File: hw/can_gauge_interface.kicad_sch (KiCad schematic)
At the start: 61 parts, among them J1 Conn_02x04_Top_Bottom, J2 Analog, J3 Power debug, J4 Power debug, J5 SPI debug, J6 I^{2}C debug, J7 CAN debug, J8 SWD, U1 STM32C092CBT6, U2 TPS5430DDA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

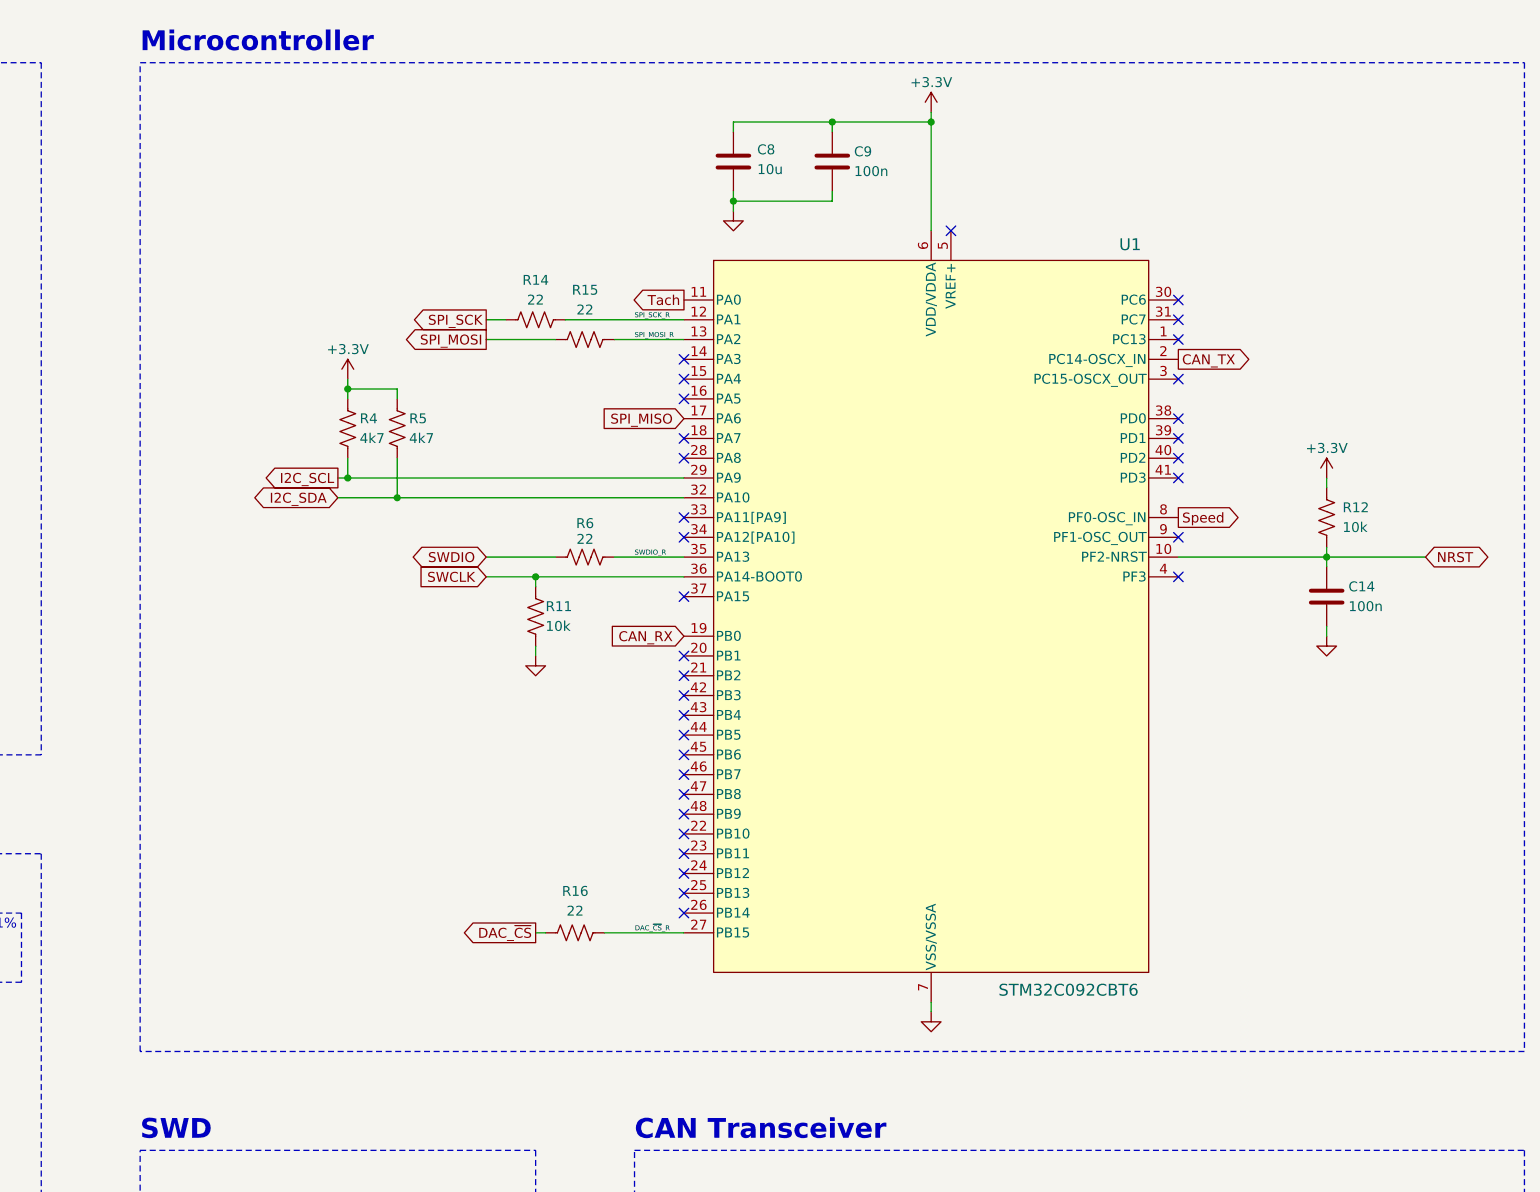
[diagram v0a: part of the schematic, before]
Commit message: hw: microcontroller hierarchical sheet
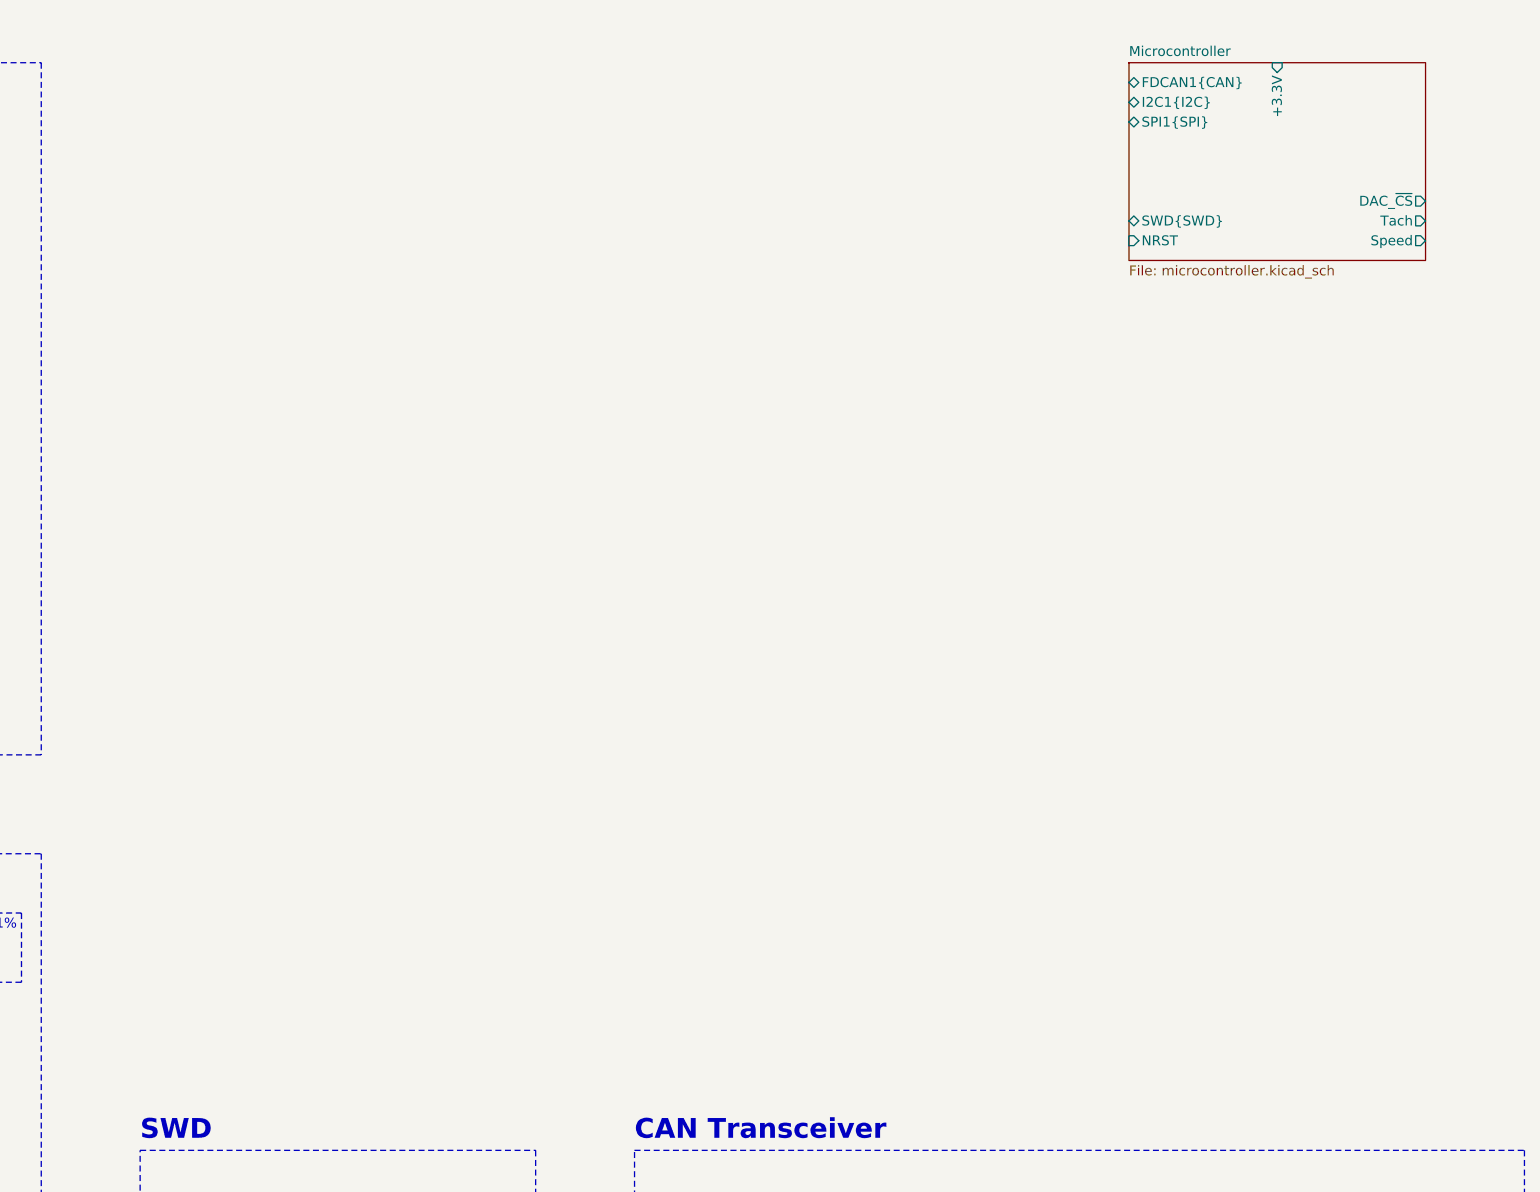
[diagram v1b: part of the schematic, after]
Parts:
- removed C14, C9: 100n, Capacitor_SMD:C_0402_1005Metric, symbol Device:C
- removed C8: 10u, Capacitor_SMD:C_0805_2012Metric, symbol Device:C
- removed R11, R12: 10k, Resistor_SMD:R_0603_1608Metric, symbol Device:R_US
- removed R14, R15, R16, R6: 22, Resistor_SMD:R_0603_1608Metric, symbol Device:R_US
- removed R4, R5: 4k7, Resistor_SMD:R_0603_1608Metric, symbol Device:R_US
- removed U1: STM32C092CBT6, footprints:LQFP48_STM, symbol STM32C092CBT6:STM32C092CBT6
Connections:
- no-connect marks 38 -> 5
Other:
- added sheet Microcontroller (microcontroller.kicad_sch)
- note removed: "Microcontroller"

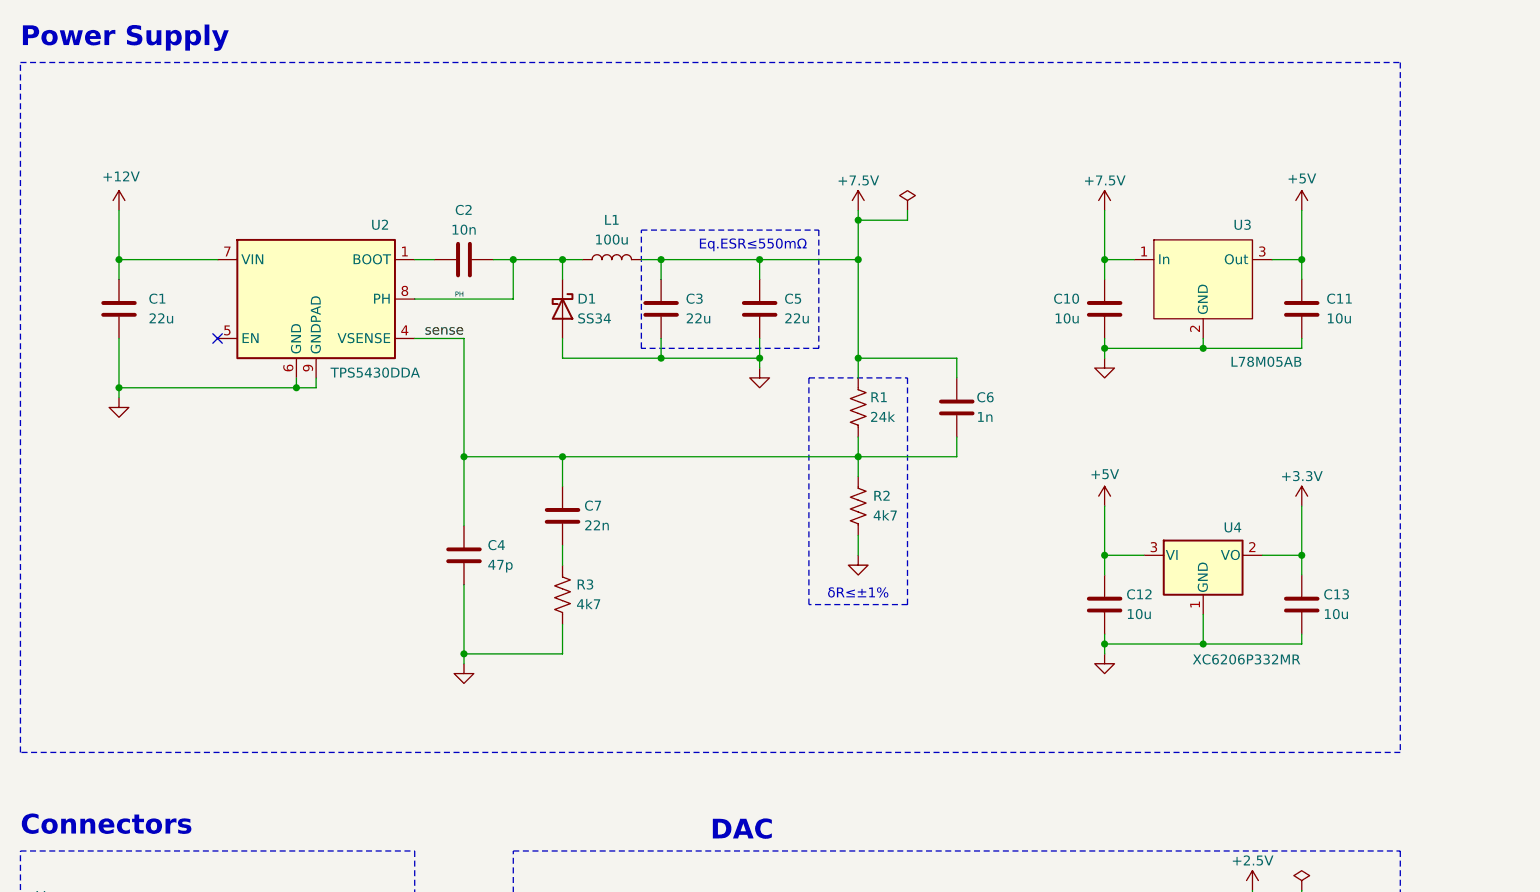
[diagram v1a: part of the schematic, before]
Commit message: hw: power supply hierarchical sheets
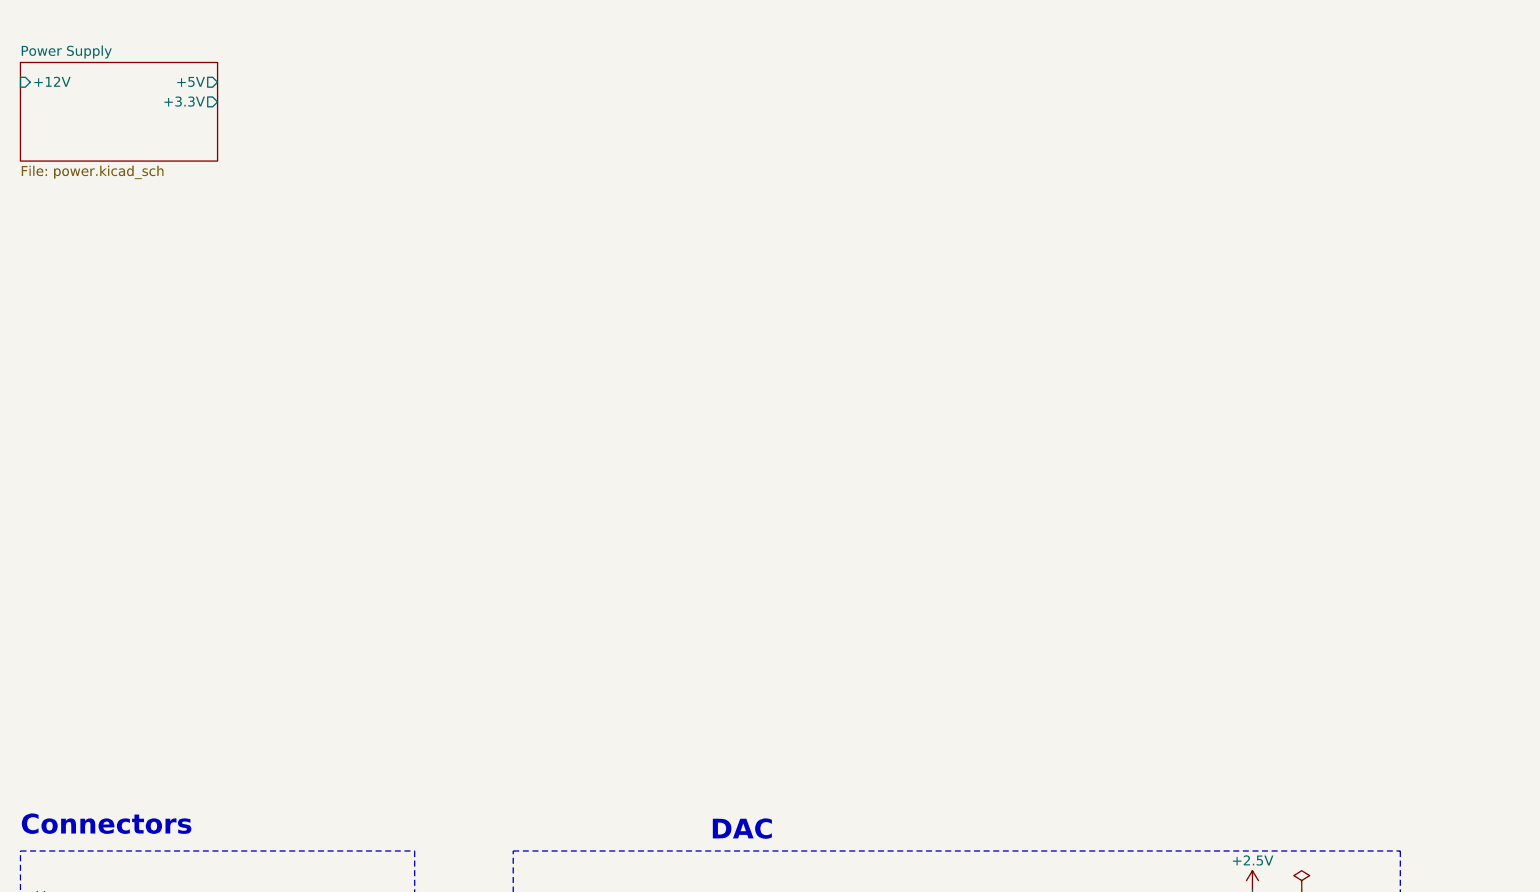
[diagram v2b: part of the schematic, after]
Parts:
- removed C1, C3, C5: 22u, Capacitor_SMD:C_1206_3216Metric, symbol Device:C
- removed C10, C11, C12, C13: 10u, Capacitor_SMD:C_0805_2012Metric, symbol Device:C
- removed C2: 10n, Capacitor_SMD:C_0402_1005Metric, symbol Device:C
- removed C4: 47p, Capacitor_SMD:C_0402_1005Metric, symbol Device:C
- removed C6: 1n, Capacitor_SMD:C_0603_1608Metric, symbol Device:C
- removed C7: 22n, Capacitor_SMD:C_0603_1608Metric, symbol Device:C
- removed D1: SS34, Diode_SMD:D_SMA, symbol Device:D_Schottky
- removed L1: 100u, Inductor_SMD:L_TaiTech_TMPC1265_13.5x12.5mm, symbol Device:L
- removed R1: 24k, Resistor_SMD:R_0603_1608Metric, symbol Device:R_US
- removed R2, R3: 4k7, Resistor_SMD:R_0603_1608Metric, symbol Device:R_US
- removed U2: TPS5430DDA, Package_SO:TI_SO-PowerPAD-8, symbol Regulator_Switching:TPS5430DDA
- removed U3: L78M05AB, Package_TO_SOT_SMD:TO-252-2, symbol symbols:L78M05AB
- removed U4: XC6206P332MR, Package_TO_SOT_SMD:SOT-23-3, symbol Regulator_Linear:XC6206PxxxMR
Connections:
- no-connect marks 5 -> 4
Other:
- added sheet Power Supply (power.kicad_sch)
- note removed: "Eq.ESR≤550mΩ"
- note removed: "Power Supply"

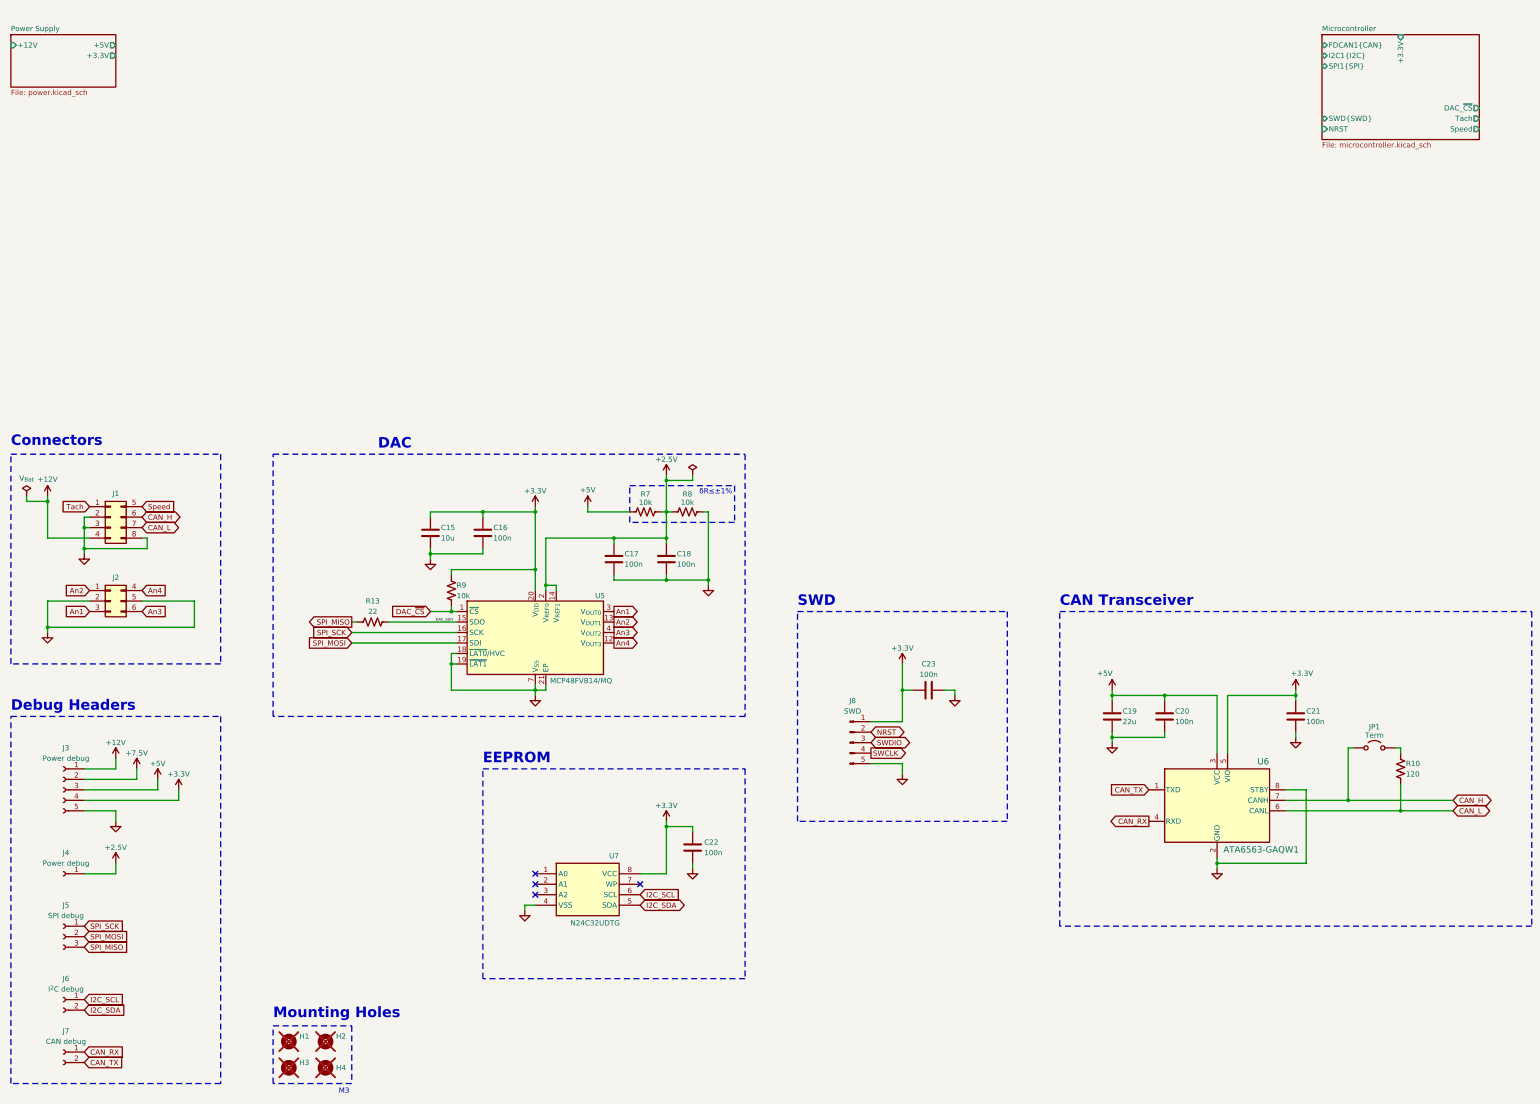
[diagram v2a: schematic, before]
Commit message: connectors hierarchical sheet
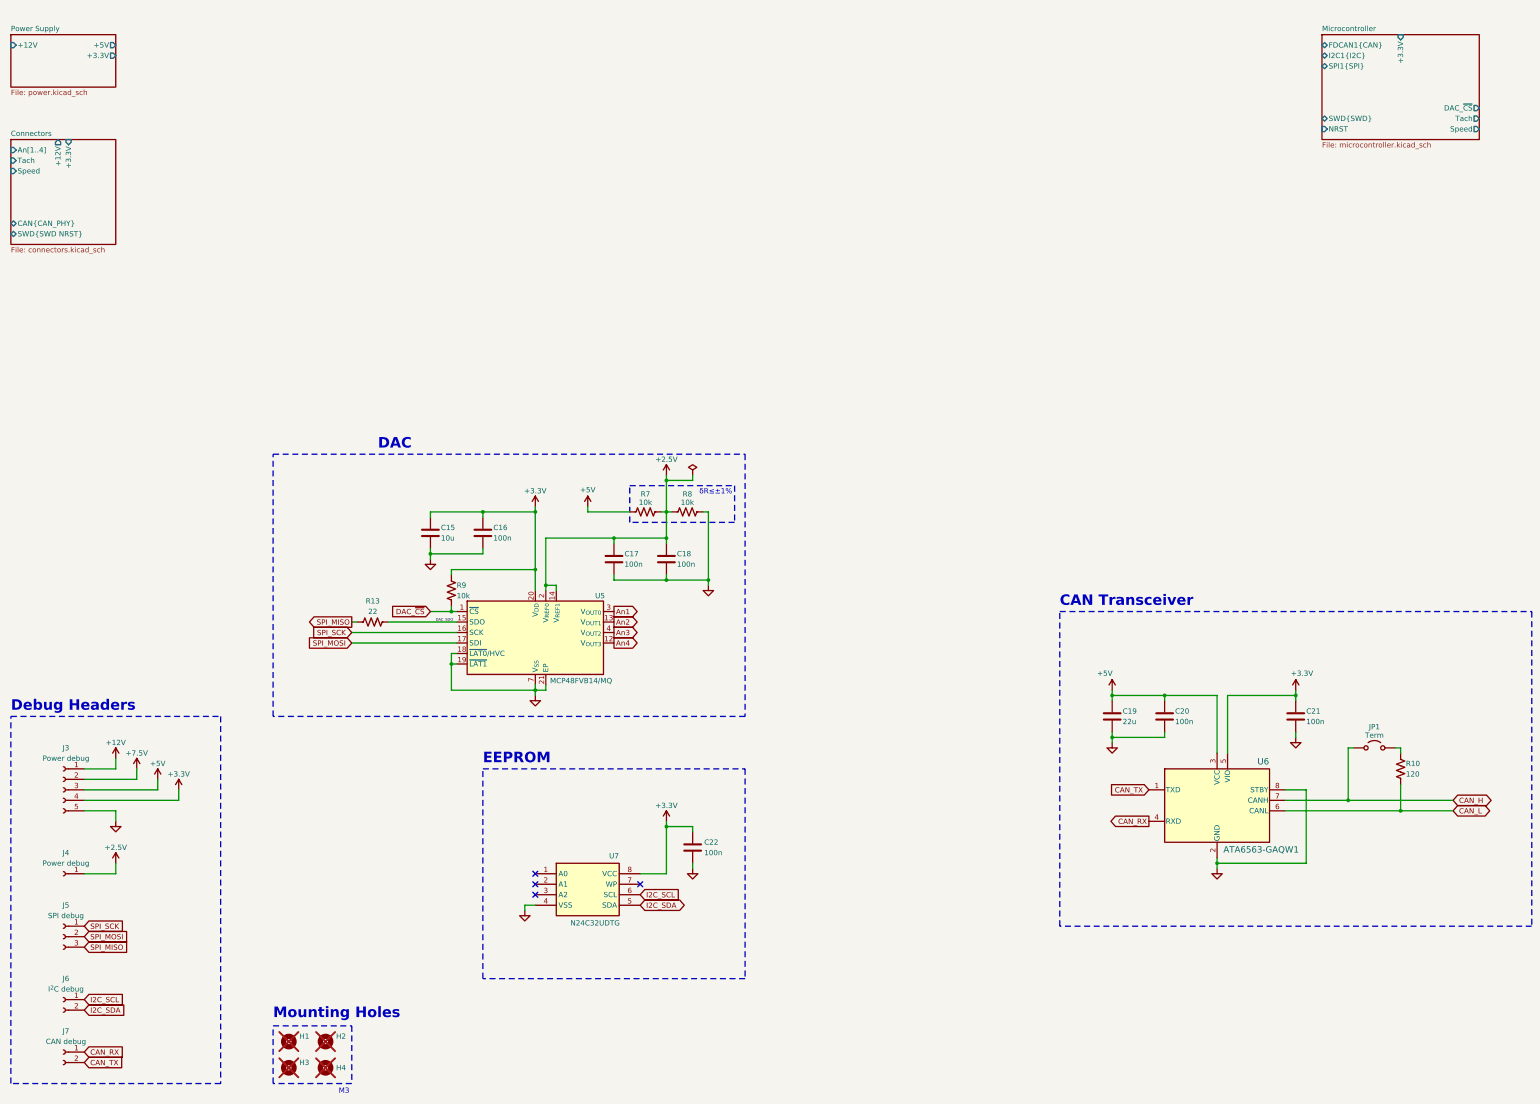
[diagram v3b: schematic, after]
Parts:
- removed C23: 100n, Capacitor_SMD:C_0402_1005Metric, symbol Device:C
- removed J1: Conn_02x04_Top_Bottom, footprints:Molex_Mini-Fit_Jr_5569-08A2_2x04_P4.20mm_Horizontal, symbol Connector_Generic:Conn_02x04_Top_Bottom
- removed J2: Analog, footprints:Molex_Mini-Fit_Jr_5569-06A2_2x03_P4.20mm_Horizontal, symbol Connector_Generic:Conn_02x03_Top_Bottom
- removed J8: SWD, Connector_PinHeader_2.54mm:PinHeader_1x05_P2.54mm_Vertical, symbol Connector:Conn_01x05_Pin
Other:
- added sheet Connectors (connectors.kicad_sch)
- note removed: "Connectors"
- note removed: "SWD"
